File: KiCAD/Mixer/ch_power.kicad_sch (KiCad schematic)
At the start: 3 parts, among them J4 Conn_02x08_Odd_Even

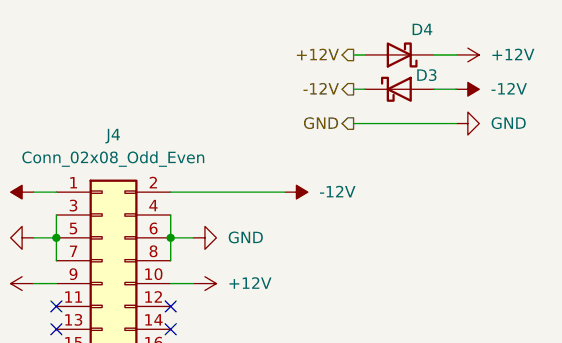
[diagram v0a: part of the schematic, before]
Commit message: added second channel and footprints / created PCB desing...might make PCB bit bigger
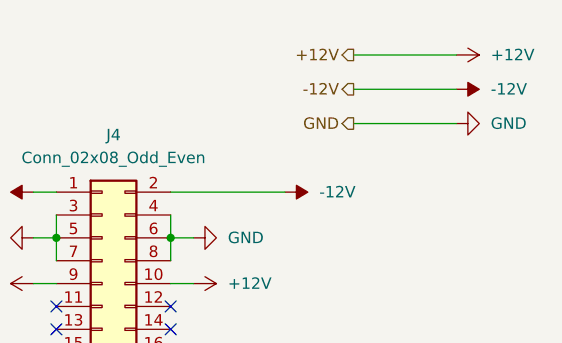
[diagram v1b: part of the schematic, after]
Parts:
- removed D3, D4: D_Schottky, Diode_SMD:D_SMA_Handsoldering, symbol Device:D_Schottky
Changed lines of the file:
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@@
-	(wire
-		(pts
-			(xy 97.79 27.94) (xy 100.33 27.94)
-		)
-		(stroke
-			(width 0)
-			(type default)
-		)
-	)
 	(wire
 		(pts
@@
 	(wire
 		(pts
-			(xy 88.9 27.94) (xy 90.17 27.94)
-		)
-		(stroke
-			(width 0)
-			(type default)
-		)
-	)
-	(wire
-		(pts
-			(xy 97.79 31.75) (xy 100.33 31.75)
-		)
-		(stroke
-			(width 0)
-			(type default)
-		)
-	)
-	(wire
-		(pts
-			(xy 88.9 31.75) (xy 90.17 31.75)
+			(xy 88.9 27.94) (xy 100.33 27.94)
+		)
+		(stroke
+			(width 0)
+			(type default)
+		)
+	)
+	(wire
+		(pts
+			(xy 88.9 31.75) (xy 100.33 31.75)
 		)
 		(stroke
@@
 	)
 	(symbol
-		(lib_id "Device:D_Schottky")
-		(at 93.98 31.75 0)
-		(unit 1)
-		(body_style 1)
-		(exclude_from_sim no)
-		(in_bom yes)
-		(on_board yes)
-		(in_pos_files yes)
-		(dnp no)
-		(property "Reference" "D3"
-			(at 97.028 30.226 0)
-			(show_name no)
-			(do_not_autoplace no)
-			(effects
-				(font
-					(size 1.27 1.27)
-				)
-			)
-		)
-		(property "Value" "D_Schottky"
-			(at 93.6625 27.94 0)
-			(hide yes)
-			(show_name no)
-			(do_not_autoplace no)
-			(effects
-				(font
-					(size 1.27 1.27)
-				)
-			)
-		)
-		(property "Footprint" "Diode_SMD:D_SMA_Handsoldering"
-			(at 93.98 31.75 0)
-			(hide yes)
-			(show_name no)
-			(do_not_autoplace no)
-			(effects
-				(font
-					(size 1.27 1.27)
-				)
-			)
-		)
-		(property "Datasheet" ""
-			(at 93.98 31.75 0)
-			(hide yes)
-			(show_name no)
-			(do_not_autoplace no)
-			(effects
-				(font
-					(size 1.27 1.27)
-				)
-			)
-		)
-		(property "Description" "Schottky diode"
-			(at 93.98 31.75 0)
-			(hide yes)
-			(show_name no)
-			(do_not_autoplace no)
-			(effects
-				(font
-					(size 1.27 1.27)
-				)
-			)
-		)
-		(pin "2"
-		)
-		(pin "1"
-		)
-		(instances
-			(project "Mixer"
-				(path "/322d427a-6aae-4762-92d6-d97688daf29b/8a2849b7-184d-4014-bb98-da9dec8b5f90/932feda2-710a-4894-b943-37dbe0c193d3"
-					(reference "D3")
-					(unit 1)
-				)
-			)
-		)
-	)
-	(symbol
 		(lib_id "power:+12V")
 		(at 100.33 27.94 270)
@@
 					(unit 1)
 				)
-			)
-		)
-	)
-	(symbol
-		(lib_id "Device:D_Schottky")
-		(at 93.98 27.94 180)
-		(unit 1)
-		(body_style 1)
-		(exclude_from_sim no)
-		(in_bom yes)
-		(on_board yes)
-		(in_pos_files yes)
-		(dnp no)
-		(property "Reference" "D4"
-			(at 96.52 25.146 0)
-			(show_name no)
-			(do_not_autoplace no)
-			(effects
-				(font
-					(size 1.27 1.27)
-				)
-			)
-		)
-		(property "Value" "D_Schottky"
-			(at 94.2975 24.13 0)
-			(hide yes)
-			(show_name no)
-			(do_not_autoplace no)
-			(effects
-				(font
-					(size 1.27 1.27)
-				)
-			)
-		)
-		(property "Footprint" "Diode_SMD:D_SMA_Handsoldering"
-			(at 93.98 27.94 0)
-			(hide yes)
-			(show_name no)
-			(do_not_autoplace no)
-			(effects
-				(font
-					(size 1.27 1.27)
-				)
-			)
-		)
-		(property "Datasheet" ""
-			(at 93.98 27.94 0)
-			(hide yes)
-			(show_name no)
-			(do_not_autoplace no)
-			(effects
-				(font
-					(size 1.27 1.27)
-				)
-			)
-		)
-		(property "Description" "Schottky diode"
-			(at 93.98 27.94 0)
-			(hide yes)
-			(show_name no)
-			(do_not_autoplace no)
-			(effects
-				(font
-					(size 1.27 1.27)
-				)
-			)
-		)
-		(pin "2"
-		)
-		(pin "1"
-		)
-		(instances
-			(project "Mixer"
-				(path "/322d427a-6aae-4762-92d6-d97688daf29b/8a2849b7-184d-4014-bb98-da9dec8b5f90/932feda2-710a-4894-b943-37dbe0c193d3"
-					(reference "D4")
-					(unit 1)
-				)

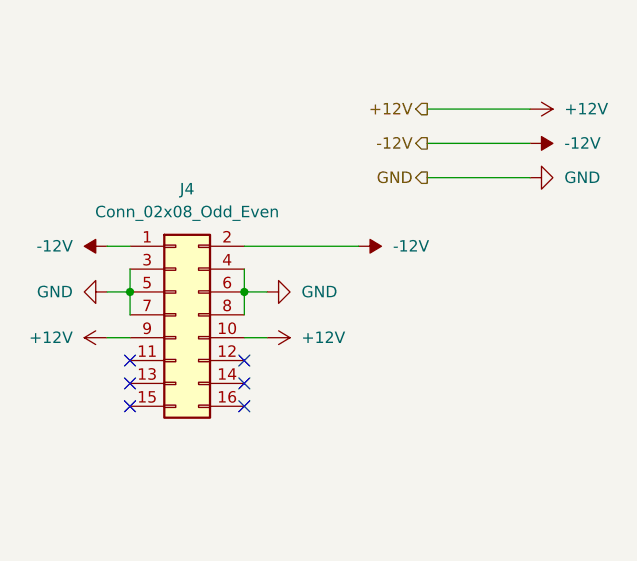
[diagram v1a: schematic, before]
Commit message: Cs an OPV-Strom, Anpassung clicklessmute,...
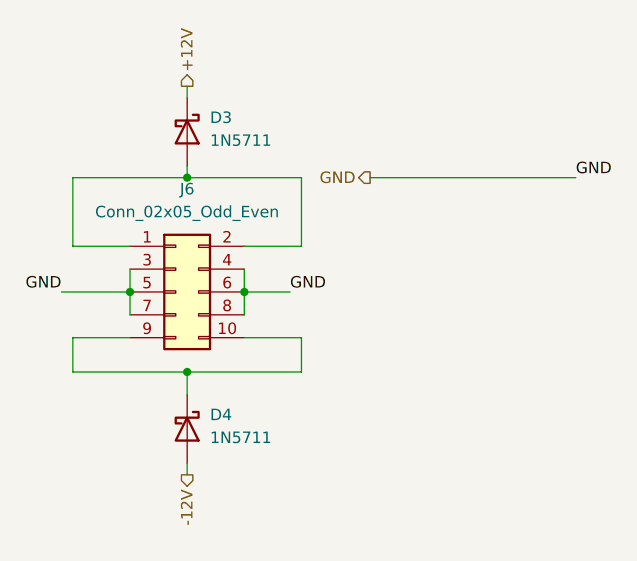
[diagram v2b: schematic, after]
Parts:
- removed J4: Conn_02x08_Odd_Even, Connector_PinHeader_2.54mm:PinHeader_2x08_P2.54mm_Vertical, symbol Connector_Generic:Conn_02x08_Odd_Even
- added D3, D4: 1N5711, Diode_THT:D_DO-35_SOD27_P7.62mm_Horizontal, symbol Diode:1N5711
- added J6: Conn_02x05_Odd_Even, Connector_PinHeader_2.54mm:PinHeader_2x05_P2.54mm_Vertical_SMD, symbol Connector_Generic:Conn_02x05_Odd_Even
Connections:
- net +12V: now also D3.1 (K)
- net -12V: now also D4.2 (A)
- net GND: now also J6.3 (Pin_3), J6.4 (Pin_4), J6.5 (Pin_5), J6.6 (Pin_6), J6.7 (Pin_7), J6.8 (Pin_8)
- new net: D3.2 (A), J6.1 (Pin_1), J6.2 (Pin_2)
- new net: D4.1 (K), J6.10 (Pin_10), J6.9 (Pin_9)
- no-connect marks 6 -> 0

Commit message: überarbeitete Schaltung und PCB Desing...v1.0 FERTIG
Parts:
- added C17, C5: 100u, Capacitor_THT:CP_Radial_D5.0mm_P2.50mm, symbol Device:C_Polarized_Small
- D3, D4: footprint Diode_THT:D_DO-35_SOD27_P7.62mm_Horizontal -> Diode_SMD:D_SMA
- J6: footprint Connector_PinHeader_2.54mm:PinHeader_2x05_P2.54mm_Vertical_SMD -> Connector_PinHeader_2.54mm:PinHeader_2x05_P2.54mm_Vertical
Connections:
- net GND: now also C17.2, C5.1
- net at D3.2 (A), J6.1 (Pin_1), J6.2 (Pin_2): now also C17.1
- net at D4.1 (K), J6.10 (Pin_10), J6.9 (Pin_9): now also C5.2
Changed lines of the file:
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@@
 	(paper "A4")
+	(junction
+		(at 74.93 57.15)
+		(diameter 0)
+		(color 0 0 0 0)
+	)
+	(junction
+		(at 74.93 35.56)
+		(diameter 0)
+		(color 0 0 0 0)
+	)
 	(junction
 		(at 62.23 35.56)
@@
 	(wire
 		(pts
-			(xy 82.55 35.56) (xy 105.41 35.56)
+			(xy 96.52 35.56) (xy 105.41 35.56)
 		)
 		(stroke
@@
 	)
 	(label "GND"
+		(at 74.93 30.48 0)
+		(effects
+			(font
+				(size 1.27 1.27)
+			)
+			(justify left bottom)
+		)
+	)
+	(label "GND"
 		(at 48.26 48.26 180)
+		(effects
+			(font
+				(size 1.27 1.27)
+			)
+			(justify right bottom)
+		)
+	)
+	(label "GND"
+		(at 74.93 62.23 270)
 		(effects
 			(font
@@
 	(hierarchical_label "GND"
 		(shape output)
-		(at 82.55 35.56 180)
+		(at 96.52 35.56 180)
 		(effects
 			(font
@@
 			)
 			(justify left)
+		)
+	)
+	(symbol
+		(lib_id "Device:C_Polarized_Small")
+		(at 74.93 33.02 180)
+		(unit 1)
+		(body_style 1)
+		(exclude_from_sim no)
+		(in_bom yes)
+		(on_board yes)
+		(in_pos_files yes)
+		(dnp no)
+		(fields_autoplaced yes)
+		(property "Reference" "C17"
+			(at 77.47 32.2961 0)
+			(show_name no)
+			(do_not_autoplace no)
+			(effects
+				(font
+					(size 1.27 1.27)
+				)
+				(justify right)
+			)
+		)
+		(property "Value" "100u"
+			(at 77.47 34.8361 0)
+			(show_name no)
+			(do_not_autoplace no)
+			(effects
+				(font
+					(size 1.27 1.27)
+				)
+				(justify right)
+			)
+		)
+		(property "Footprint" "Capacitor_THT:CP_Radial_D5.0mm_P2.50mm"
+			(at 74.93 33.02 0)
+			(hide yes)
+			(show_name no)
+			(do_not_autoplace no)
+			(effects
+				(font
+					(size 1.27 1.27)
+				)
+			)
+		)
+		(property "Datasheet" ""
+			(at 74.93 33.02 0)
+			(hide yes)
+			(show_name no)
+			(do_not_autoplace no)
+			(effects
+				(font
+					(size 1.27 1.27)
+				)
+			)
+		)
+		(property "Description" "Polarized capacitor, small symbol"
+			(at 74.93 33.02 0)
+			(hide yes)
+			(show_name no)
+			(do_not_autoplace no)
+			(effects
+				(font
+					(size 1.27 1.27)
+				)
+			)
+		)
+		(pin "1"
+		)
+		(pin "2"
+		)
+		(instances
+			(project "Mixer"
+				(path "/322d427a-6aae-4762-92d6-d97688daf29b/8a2849b7-184d-4014-bb98-da9dec8b5f90/932feda2-710a-4894-b943-37dbe0c193d3"
+					(reference "C17")
+					(unit 1)
+				)
+			)
 		)
 	)
@@
 			)
 		)
-		(property "Footprint" "Diode_THT:D_DO-35_SOD27_P7.62mm_Horizontal"
+		(property "Footprint" "Diode_SMD:D_SMA"
 			(at 57.785 30.48 0)
 			(hide yes)
@@
 		(property "Value" "Conn_02x05_Odd_Even"
 			(at 62.23 39.37 0)
-			(show_name no)
-			(do_not_autoplace no)
-			(effects
-				(font
-					(size 1.27 1.27)
-				)
-			)
-		)
-		(property "Footprint" "Connector_PinHeader_2.54mm:PinHeader_2x05_P2.54mm_Vertical_SMD"
+			(hide yes)
+			(show_name no)
+			(do_not_autoplace no)
+			(effects
+				(font
+					(size 1.27 1.27)
+				)
+			)
+		)
+		(property "Footprint" "Connector_PinHeader_2.54mm:PinHeader_2x05_P2.54mm_Vertical"
 			(at 60.96 48.26 0)
 			(hide yes)
@@
 				(path "/322d427a-6aae-4762-92d6-d97688daf29b/8a2849b7-184d-4014-bb98-da9dec8b5f90/932feda2-710a-4894-b943-37dbe0c193d3"
 					(reference "J6")
+					(unit 1)
+				)
+			)
+		)
+	)
+	(symbol
+		(lib_id "Device:C_Polarized_Small")
+		(at 74.93 59.69 0)
+		(mirror x)
+		(unit 1)
+		(body_style 1)
+		(exclude_from_sim no)
+		(in_bom yes)
+		(on_board yes)
+		(in_pos_files yes)
+		(dnp no)
+		(property "Reference" "C5"
+			(at 77.47 61.5061 0)
+			(show_name no)
+			(do_not_autoplace no)
+			(effects
+				(font
+					(size 1.27 1.27)
+				)
+				(justify left)
+			)
+		)
+		(property "Value" "100u"
+			(at 77.47 58.9661 0)
+			(show_name no)
+			(do_not_autoplace no)
+			(effects
+				(font
+					(size 1.27 1.27)
+				)
+				(justify left)
+			)
+		)
+		(property "Footprint" "Capacitor_THT:CP_Radial_D5.0mm_P2.50mm"
+			(at 74.93 59.69 0)
+			(hide yes)
+			(show_name no)
+			(do_not_autoplace no)
+			(effects
+				(font
+					(size 1.27 1.27)
+				)
+			)
+		)
+		(property "Datasheet" ""
+			(at 74.93 59.69 0)
+			(hide yes)
+			(show_name no)
+			(do_not_autoplace no)
+			(effects
+				(font
+					(size 1.27 1.27)
+				)
+			)
+		)
+		(property "Description" "Polarized capacitor, small symbol"
+			(at 74.93 59.69 0)
+			(hide yes)
+			(show_name no)
+			(do_not_autoplace no)
+			(effects
+				(font
+					(size 1.27 1.27)
+				)
+			)
+		)
+		(pin "1"
+		)
+		(pin "2"
+		)
+		(instances
+			(project "Mixer"
+				(path "/322d427a-6aae-4762-92d6-d97688daf29b/8a2849b7-184d-4014-bb98-da9dec8b5f90/932feda2-710a-4894-b943-37dbe0c193d3"
+					(reference "C5")
 					(unit 1)
 				)
@@
 			)
 		)
-		(property "Footprint" "Diode_THT:D_DO-35_SOD27_P7.62mm_Horizontal"
+		(property "Footprint" "Diode_SMD:D_SMA"
 			(at 57.785 63.5 0)
 			(hide yes)

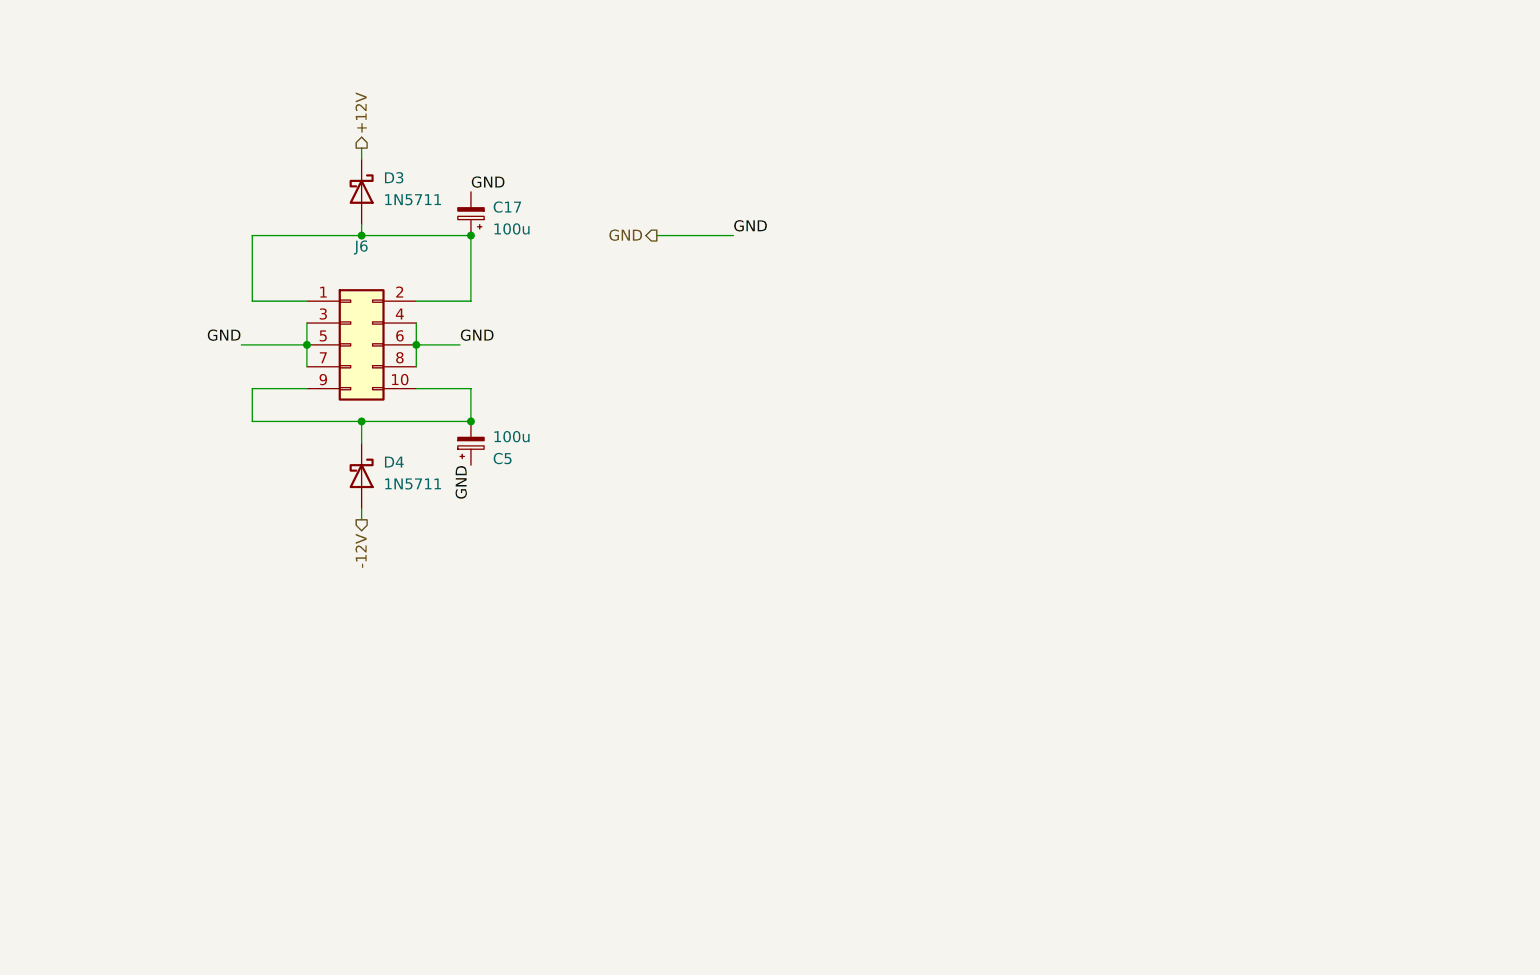
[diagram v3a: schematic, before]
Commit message: Rework of schematic, with error fixes and reworked pcb
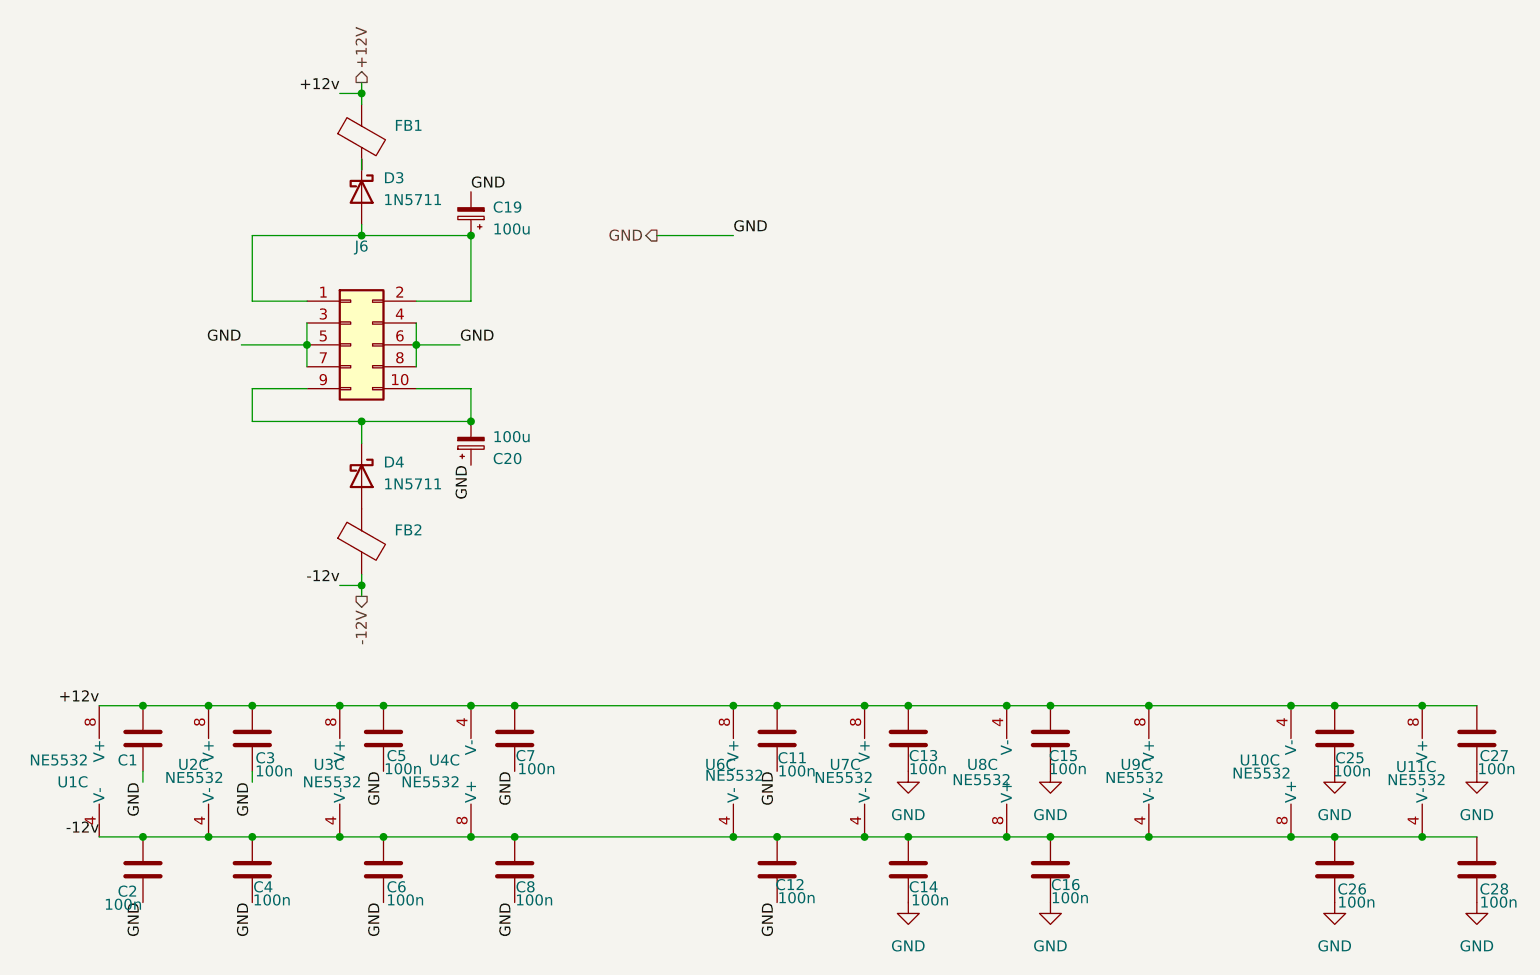
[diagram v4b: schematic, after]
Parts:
- added C1, C11, C12, C13, C14, C15, C16, C2, C25, C26, C27, C28, C3, C4, C5, C6, C7, C8: 100n, Capacitor_SMD:C_0805_2012Metric_Pad1.18x1.45mm_HandSolder, symbol Device:C
- added FB1, FB2: FerriteBead, Inductor_SMD:L_0805_2012Metric_Pad1.05x1.20mm_HandSolder, symbol Device:FerriteBead
- added U1, U10, U11, U2, U3, U4, U6, U7, U8, U9: NE5532, Package_SO:SOIC-8_3.9x4.9mm_P1.27mm, symbol Amplifier_Operational:NE5532
- C19: renamed from C17; footprint Capacitor_THT:CP_Radial_D5.0mm_P2.50mm -> 2917_Tantal_Elko:CAPPM7343X310N
- C20: renamed from C5; footprint Capacitor_THT:CP_Radial_D5.0mm_P2.50mm -> 2917_Tantal_Elko:CAPPM7343X310N
- D3, D4: footprint Diode_SMD:D_SMA -> Diode_SMD:D_MiniMELF
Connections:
- net +12V: now also C1.2, C11.2, C13.2, C15.2, C25.2, C27.2, C3.2, C5.2, C7.2, FB1.1, U1.8 (V+), U10.4 (V-), U11.8 (V+), U2.8 (V+), U3.8 (V+), U4.4 (V-), U6.8 (V+), U7.8 (V+), U8.4 (V-), U9.8 (V+); no longer D3.1 (K)
- net -12V: now also C12.2, C14.2, C16.2, C2.2, C26.2, C28.2, C4.2, C6.2, C8.2, FB2.2, U1.4 (V-), U10.8 (V+), U11.4 (V-), U2.4 (V-), U3.4 (V-), U4.8 (V+), U6.4 (V-), U7.4 (V-), U8.8 (V+), U9.4 (V-); no longer D4.2 (A)
- net GND: now also C1.1, C11.1, C12.1, C13.1, C14.1, C15.1, C16.1, C2.1, C25.1, C26.1, C27.1, C28.1, C3.1, C4.1, C5.1, C6.1, C7.1, C8.1
- new net: D3.1 (K), FB1.2
- new net: D4.2 (A), FB2.1

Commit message: Final PCB Version that got ordered from JLCPCB
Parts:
- added C13, C14: 100n, Capacitor_SMD:C_0805_2012Metric_Pad1.18x1.45mm_HandSolder, symbol Device:C
- D3, D4: footprint Diode_SMD:D_MiniMELF -> Diode_SMD:D_SOD-123
- renumbered C20 to C10, C7 to C11, C8 to C12, C11 to C15, C12 to C16, C13 to C17, C14 to C18, C15 to C19, C16 to C20, C25 to C21, C26 to C22, C27 to C23, C28 to C24, C1 to C3, C2 to C4, C3 to C5, C4 to C6, C5 to C7, C6 to C8, C19 to C9, U3 to U10, U4 to U2, U2 to U3, U8 to U4, U10 to U5, U9 to U6, U11 to U7, U6 to U8, U7 to U9
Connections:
- net +12V: now also C13.2
- net -12V: now also C14.2
